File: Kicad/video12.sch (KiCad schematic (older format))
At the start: 18 parts, among them J401 DE15HD, U401 THS7316, U402 TPD7S019

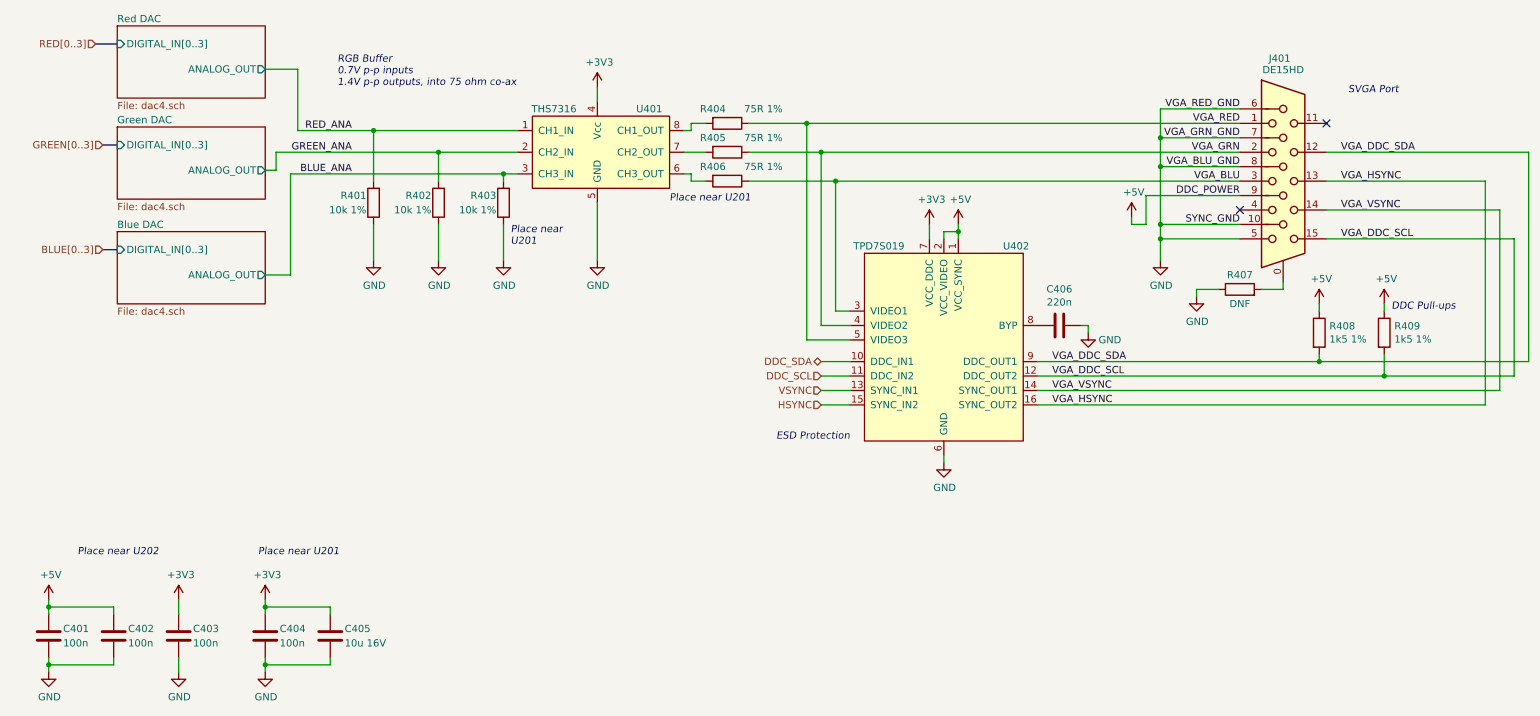
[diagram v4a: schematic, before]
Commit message: BoM and PCB fixes.
* Move tolerances and voltages out of value and into their own fields.
* Fix 5V trace for audio stage.
* Fixup docs.yml so outputs work for JLCPCB.
* Fix JLCPCB part number for 22pF caps.
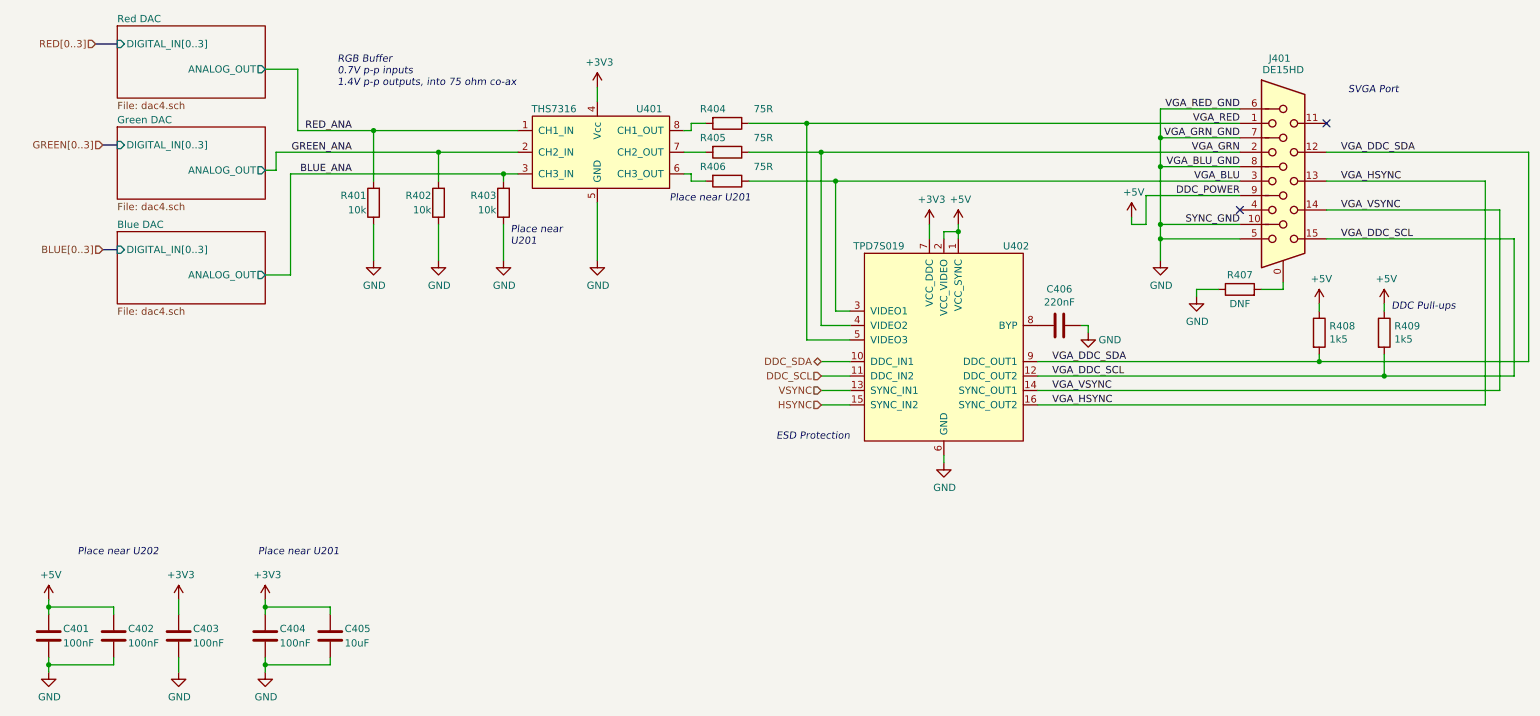
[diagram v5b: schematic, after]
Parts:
- C401, C402, C403, C404: value 100n -> 100nF
- C405: value 10u 16V -> 10uF
- C406: value 220n -> 220nF
- R401, R402, R403: value 10k 1% -> 10k
- R404, R405, R406: value 75R 1% -> 75R
- R408, R409: value 1k5 1% -> 1k5
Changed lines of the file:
@@
 P 5500 3600
 F 0 "R404" V 5400 3500 50  0000 C CNN
-F 1 "75R 1%" V 5400 3850 50  0000 C CNN
+F 1 "75R" V 5400 3850 50  0000 C CNN
 F 2 "Resistor_SMD:R_0805_2012Metric_Pad1.20x1.40mm_HandSolder" V 5430 3600 50  0001 C CNN
 F 3 "~" H 5500 3600 50  0001 C CNN
@@
 P 5500 3800
 F 0 "R405" V 5400 3700 50  0000 C CNN
-F 1 "75R 1%" V 5400 4050 50  0000 C CNN
+F 1 "75R" V 5400 4050 50  0000 C CNN
 F 2 "Resistor_SMD:R_0805_2012Metric_Pad1.20x1.40mm_HandSolder" V 5430 3800 50  0001 C CNN
 F 3 "~" H 5500 3800 50  0001 C CNN
@@
 P 5500 4000
 F 0 "R406" V 5400 3900 50  0000 C CNN
-F 1 "75R 1%" V 5400 4250 50  0000 C CNN
+F 1 "75R" V 5400 4250 50  0000 C CNN
 F 2 "Resistor_SMD:R_0805_2012Metric_Pad1.20x1.40mm_HandSolder" V 5430 4000 50  0001 C CNN
 F 3 "~" H 5500 4000 50  0001 C CNN
@@
 P 3050 4150
 F 0 "R401" H 3100 4100 50  0000 L CNN
-F 1 "10k 1%" H 3100 4200 50  0000 L CNN
+F 1 "10k" H 3100 4200 50  0000 L CNN
 F 2 "Resistor_SMD:R_0805_2012Metric_Pad1.20x1.40mm_HandSolder" V 2980 4150 50  0001 C CNN
 F 3 "~" H 3050 4150 50  0001 C CNN
@@
 P 3500 4150
 F 0 "R402" H 3550 4100 50  0000 L CNN
-F 1 "10k 1%" H 3550 4200 50  0000 L CNN
+F 1 "10k" H 3550 4200 50  0000 L CNN
 F 2 "Resistor_SMD:R_0805_2012Metric_Pad1.20x1.40mm_HandSolder" V 3430 4150 50  0001 C CNN
 F 3 "~" H 3500 4150 50  0001 C CNN
@@
 P 3950 4150
 F 0 "R403" H 4000 4100 50  0000 L CNN
-F 1 "10k 1%" H 4000 4200 50  0000 L CNN
+F 1 "10k" H 4000 4200 50  0000 L CNN
 F 2 "Resistor_SMD:R_0805_2012Metric_Pad1.20x1.40mm_HandSolder" V 3880 4150 50  0001 C CNN
 F 3 "~" H 3950 4150 50  0001 C CNN
@@
 P 9600 5050
 F 0 "R408" H 9670 5096 50  0000 L CNN
-F 1 "1k5 1%" H 9670 5005 50  0000 L CNN
+F 1 "1k5" H 9670 5005 50  0000 L CNN
 F 2 "Resistor_SMD:R_0805_2012Metric_Pad1.20x1.40mm_HandSolder" V 9530 5050 50  0001 C CNN
 F 3 "~" H 9600 5050 50  0001 C CNN
@@
 P 10050 5050
 F 0 "R409" H 10120 5096 50  0000 L CNN
-F 1 "1k5 1%" H 10120 5005 50  0000 L CNN
+F 1 "1k5" H 10120 5005 50  0000 L CNN
 F 2 "Resistor_SMD:R_0805_2012Metric_Pad1.20x1.40mm_HandSolder" V 9980 5050 50  0001 C CNN
 F 3 "~" H 10050 5050 50  0001 C CNN
@@
 P 7800 5000
 F 0 "C406" V 7548 5000 50  0000 C CNN
-F 1 "220n" V 7639 5000 50  0000 C CNN
+F 1 "220nF" V 7639 5000 50  0000 C CNN
 F 2 "Capacitor_SMD:C_0805_2012Metric_Pad1.18x1.45mm_HandSolder" H 7838 4850 50  0001 C CNN
 F 3 "~" H 7800 5000 50  0001 C CNN
@@
 P 800 7150
 F 0 "C401" H 700 7100 50  0000 R CNN
-F 1 "100n" H 700 7200 50  0000 R CNN
+F 1 "100nF" H 700 7200 50  0000 R CNN
 F 2 "Capacitor_SMD:C_0805_2012Metric_Pad1.18x1.45mm_HandSolder" H 838 7000 50  0001 C CNN
 F 3 "~" H 800 7150 50  0001 C CNN
@@
 P 1250 7150
 F 0 "C402" H 1150 7100 50  0000 R CNN
-F 1 "100n" H 1150 7200 50  0000 R CNN
+F 1 "100nF" H 1150 7200 50  0000 R CNN
 F 2 "Capacitor_SMD:C_0805_2012Metric_Pad1.18x1.45mm_HandSolder" H 1288 7000 50  0001 C CNN
 F 3 "~" H 1250 7150 50  0001 C CNN
@@
 P 2300 7150
 F 0 "C404" H 2200 7100 50  0000 R CNN
-F 1 "100n" H 2200 7200 50  0000 R CNN
+F 1 "100nF" H 2200 7200 50  0000 R CNN
 F 2 "Capacitor_SMD:C_0805_2012Metric_Pad1.18x1.45mm_HandSolder" H 2338 7000 50  0001 C CNN
 F 3 "~" H 2300 7150 50  0001 C CNN
@@
 P 2750 7150
 F 0 "C405" H 2650 7200 50  0000 R CNN
-F 1 "10u 16V" H 2650 7100 50  0000 R CNN
+F 1 "10uF" H 2650 7100 50  0000 R CNN
 F 2 "Capacitor_SMD:C_0805_2012Metric_Pad1.18x1.45mm_HandSolder" H 2788 7000 50  0001 C CNN
 F 3 "~" H 2750 7150 50  0001 C CNN
@@
 P 1700 7150
 F 0 "C403" H 1600 7100 50  0000 R CNN
-F 1 "100n" H 1600 7200 50  0000 R CNN
+F 1 "100nF" H 1600 7200 50  0000 R CNN
 F 2 "Capacitor_SMD:C_0805_2012Metric_Pad1.18x1.45mm_HandSolder" H 1738 7000 50  0001 C CNN
 F 3 "~" H 1700 7150 50  0001 C CNN

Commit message: Bugfix/replace vga connector (#20)
* Starting to replace VGA connector.

The Amphenol connectors used on Monotron and the Neotron 32 have a
roughly 8.5mm offset to the board edge. Fixing this will involve moving
a lot of stuff.

* Finish adding new VGA connector.

Had to bunch up the R2R DACs a bit, but overall
it seems tidier this time!
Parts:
- J401: footprint Connector_Dsub:DSUB-15-HD_Female_Horizontal_P2.29x1.98mm_EdgePinOffset3.03mm_Housed_MountingHolesOffset4.94mm -> neotron-pico:Amphenol_ICD15S13E4GV00LF
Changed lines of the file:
@@
 F 0 "J401" H 9250 4850 50  0000 L CNN
 F 1 "DE15HD" H 9350 4800 50  0000 C TNN
-F 2 "Connector_Dsub:DSUB-15-HD_Female_Horizontal_P2.29x1.98mm_EdgePinOffset3.03mm_Housed_MountingHolesOffset4.94mm" H 8400 4400 50  0001 C CNN
+F 2 "neotron-pico:Amphenol_ICD15S13E4GV00LF" H 8400 4400 50  0001 C CNN
 F 3 "~" H 8400 4400 50  0001 C CNN
 F 4 "0" H 9350 4000 50  0001 C CNN "DNP"

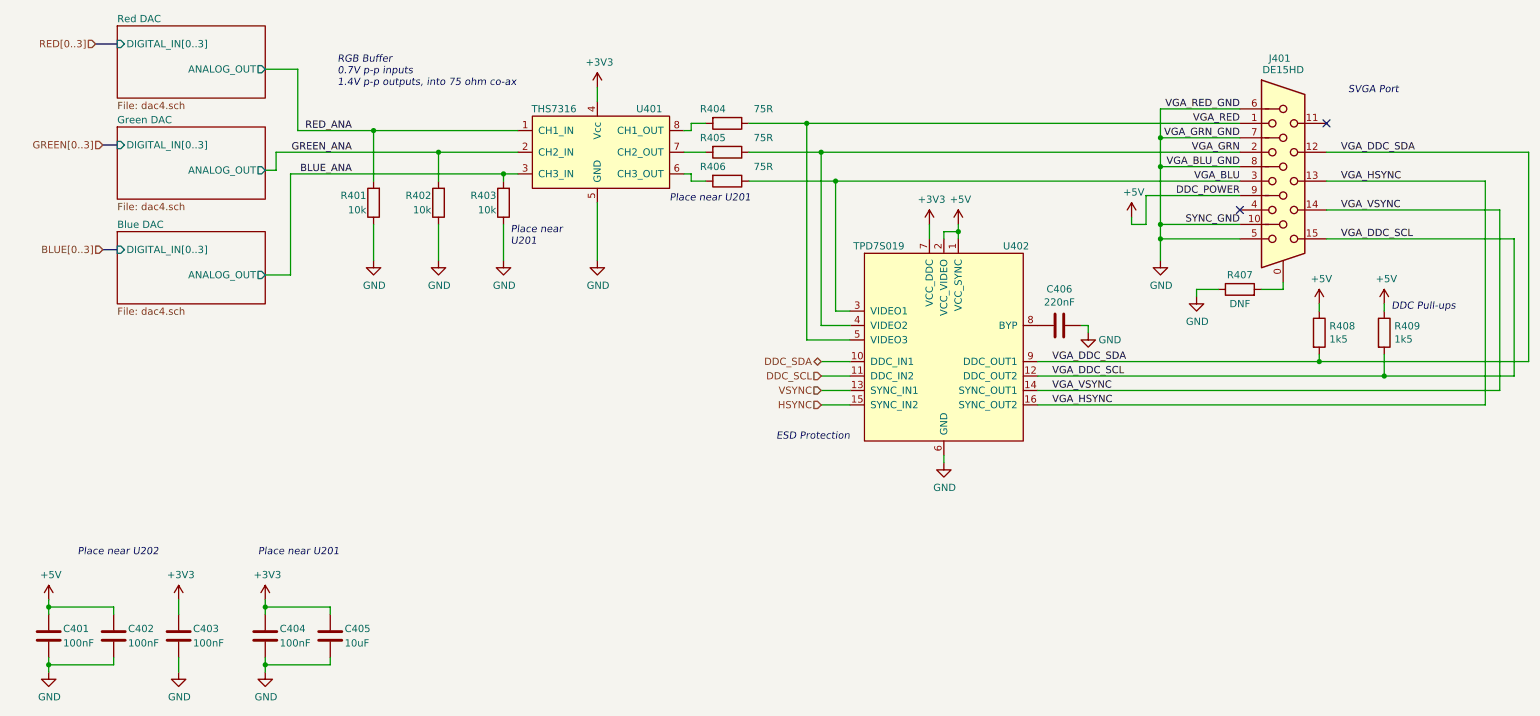
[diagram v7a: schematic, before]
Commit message: Update component values.
Tolerance and Voltage are set to the minimum acceptable. The selected
parts can be better, where a better part is cheaper or has
better availability.

Also dropped R2R DAC tolerance to 1% - 0.5% was overkill. The output
resistor had the wrong value too, which is fixed.
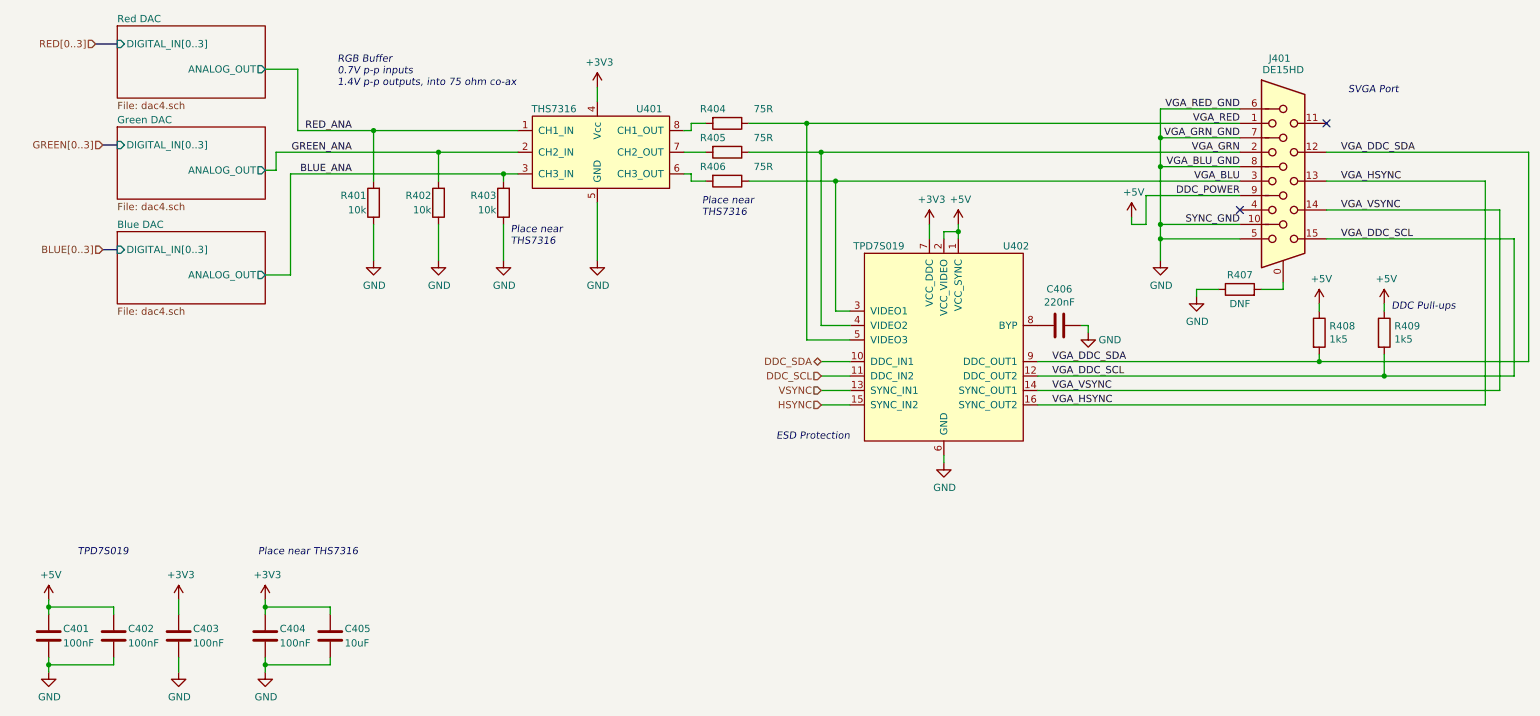
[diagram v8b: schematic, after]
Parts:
- C401, C402: Tolerance (none) -> X5R; Voltage (none) -> 16V
- C403, C404, C405: Tolerance (none) -> X5R; Voltage (none) -> 10V
- C406: Tolerance (none) -> X5R; Voltage (none) -> 50V
- R401, R402, R403, R404, R405, R406, R408, R409: Tolerance (none) -> 1%
- U401: MPN THS7316 -> THS7316DR
- U402: MPN TPD7S019 -> TPD7S019-15DBQR
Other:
- note added: "Place near THS7316"
- note added: "Place near\nTHS7316"
- note added: "TPD7S019"
- note removed: "Place near U201"
- note removed: "Place near U202"
- note removed: "Place near\nU201"
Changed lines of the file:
@@
 F 8 "649-ICD15S13E4GV00LF" H 9350 4000 50  0001 C CNN "Mouser"
 F 9 "~" H 9350 4000 50  0001 C CNN "LCSC Part#"
+F 10 "~" H 9350 4000 50  0001 C CNN "Tolerance"
+F 11 "~" H 9350 4000 50  0001 C CNN "Voltage"
 	1    9350 4000
 	1    0    0    -1
@@
 F 7 "Stackpole" H 5500 3600 50  0001 C CNN "Manufacturer"
 F 8 "C20638" H 5500 3600 50  0001 C CNN "LCSC Part#"
+F 9 "1%" H 5500 3600 50  0001 C CNN "Tolerance"
+F 10 "~" H 5500 3600 50  0001 C CNN "Voltage"
 	1    5500 3600
 	0    1    1    0
@@
 F 7 "Stackpole" H 5500 3800 50  0001 C CNN "Manufacturer"
 F 8 "C20638" H 5500 3800 50  0001 C CNN "LCSC Part#"
+F 9 "1%" H 5500 3800 50  0001 C CNN "Tolerance"
+F 10 "~" H 5500 3800 50  0001 C CNN "Voltage"
 	1    5500 3800
 	0    1    1    0
@@
 F 7 "Stackpole" H 5500 4000 50  0001 C CNN "Manufacturer"
 F 8 "C20638" H 5500 4000 50  0001 C CNN "LCSC Part#"
+F 9 "1%" H 5500 4000 50  0001 C CNN "Tolerance"
+F 10 "~" H 5500 4000 50  0001 C CNN "Voltage"
 	1    5500 4000
 	0    1    1    0
@@
 F 3 "~" H 3050 4150 50  0001 C CNN
 F 4 "0" H 3050 4150 50  0001 C CNN "DNP"
-F 5 "" H 3050 4150 50  0001 C CNN "Digikey"
+F 5 "~" H 3050 4150 50  0001 C CNN "Digikey"
 F 6 "CPL-RES-0805-10K-0.125W" H 3050 4150 50  0001 C CNN "MPN"
 F 7 "CPL" H 3050 4150 50  0001 C CNN "Manufacturer"
 F 8 "C17414" H 3050 4150 50  0001 C CNN "LCSC Part#"
+F 9 "1%" H 3050 4150 50  0001 C CNN "Tolerance"
+F 10 "~" H 3050 4150 50  0001 C CNN "Mouser"
+F 11 "~" H 3050 4150 50  0001 C CNN "Voltage"
 	1    3050 4150
 	-1   0    0    1
@@
 F 3 "~" H 3500 4150 50  0001 C CNN
 F 4 "0" H 3500 4150 50  0001 C CNN "DNP"
-F 5 "" H 3500 4150 50  0001 C CNN "Digikey"
+F 5 "~" H 3500 4150 50  0001 C CNN "Digikey"
 F 6 "CPL-RES-0805-10K-0.125W" H 3500 4150 50  0001 C CNN "MPN"
 F 7 "CPL" H 3500 4150 50  0001 C CNN "Manufacturer"
 F 8 "C17414" H 3500 4150 50  0001 C CNN "LCSC Part#"
+F 9 "1%" H 3500 4150 50  0001 C CNN "Tolerance"
+F 10 "~" H 3500 4150 50  0001 C CNN "Mouser"
+F 11 "~" H 3500 4150 50  0001 C CNN "Voltage"
 	1    3500 4150
 	-1   0    0    1
@@
 F 3 "~" H 3950 4150 50  0001 C CNN
 F 4 "0" H 3950 4150 50  0001 C CNN "DNP"
-F 5 "" H 3950 4150 50  0001 C CNN "Digikey"
+F 5 "~" H 3950 4150 50  0001 C CNN "Digikey"
 F 6 "CPL-RES-0805-10K-0.125W" H 3950 4150 50  0001 C CNN "MPN"
 F 7 "CPL" H 3950 4150 50  0001 C CNN "Manufacturer"
 F 8 "C17414" H 3950 4150 50  0001 C CNN "LCSC Part#"
+F 9 "1%" H 3950 4150 50  0001 C CNN "Tolerance"
+F 10 "~" H 3950 4150 50  0001 C CNN "Mouser"
+F 11 "~" H 3950 4150 50  0001 C CNN "Voltage"
 	1    3950 4150
 	-1   0    0    1
@@
 F 3 "https://www.ti.com/lit/ds/symlink/tpd7s019.pdf" H 7550 5200 50  0001 C CNN
 F 4 "Texas Instruments" H 7000 3750 50  0001 C CNN "Manufacturer"
-F 5 "TPD7S019" H 7000 3650 50  0001 C CNN "MPN"
+F 5 "TPD7S019-15DBQR" H 7000 3650 50  0001 C CNN "MPN"
 F 6 "0" H 7000 5100 50  0001 C CNN "DNP"
 F 7 "296-27595-1-ND" H 7000 5100 50  0001 C CNN "Digikey"
 F 8 "595-TPD7S019-15DBQR" H 7000 5100 50  0001 C CNN "Mouser"
 F 9 "C337499" H 7000 5100 50  0001 C CNN "LCSC Part#"
+F 10 "~" H 7000 5100 50  0001 C CNN "Tolerance"
+F 11 "~" H 7000 5100 50  0001 C CNN "Voltage"
 	1    7000 5100
 	1    0    0    -1
@@
 F 5 "0" H 4750 3800 50  0001 C CNN "DNP"
 F 6 "296-26684-1-ND" H 4750 3800 50  0001 C CNN "Digikey"
-F 7 "THS7316" H 4750 3800 50  0001 C CNN "MPN"
+F 7 "THS7316DR" H 4750 3800 50  0001 C CNN "MPN"
 F 8 "595-THS7316DR" H 4750 3800 50  0001 C CNN "Mouser"
 F 9 "C155446" H 4750 3800 50  0001 C CNN "LCSC Part#"
+F 10 "~" H 4750 3800 50  0001 C CNN "Tolerance"
+F 11 "~" H 4750 3800 50  0001 C CNN "Voltage"
 	1    4750 3800
 	1    0    0    -1
@@
 F 7 "Stackpole" H 9600 5050 50  0001 C CNN "Manufacturer"
 F 8 "C4310" H 9600 5050 50  0001 C CNN "LCSC Part#"
+F 9 "1%" H 9600 5050 50  0001 C CNN "Tolerance"
+F 10 "~" H 9600 5050 50  0001 C CNN "Voltage"
 	1    9600 5050
 	1    0    0    -1
@@
 F 7 "Stackpole" H 10050 5050 50  0001 C CNN "Manufacturer"
 F 8 "C4310" H 10050 5050 50  0001 C CNN "LCSC Part#"
+F 9 "1%" H 10050 5050 50  0001 C CNN "Tolerance"
+F 10 "~" H 10050 5050 50  0001 C CNN "Voltage"
 	1    10050 5050
 	1    0    0    -1
@@
 F 7 "Samsung" H 7800 5000 50  0001 C CNN "Manufacturer"
 F 8 "C5378" H 7800 5000 50  0001 C CNN "LCSC Part#"
+F 9 "X5R" H 7800 5000 50  0001 C CNN "Tolerance"
+F 10 "50V" H 7800 5000 50  0001 C CNN "Voltage"
+F 11 "~" H 7800 5000 50  0001 C CNN "Mouser"
 	1    7800 5000
 	0    1    1    0
@@
 F 3 "~" H 800 7150 50  0001 C CNN
 F 4 "0" H 800 7150 50  0001 C CNN "DNP"
-F 5 "" H 800 7150 50  0001 C CNN "Digikey"
+F 5 "~" H 800 7150 50  0001 C CNN "Digikey"
 F 6 "CPL-CAP-X7R-0805-100NF-50V" H 800 7150 50  0001 C CNN "MPN"
 F 7 "CPL" H 800 7150 50  0001 C CNN "Manufacturer"
-F 8 "" H 800 7150 50  0001 C CNN "Mouser"
+F 8 "~" H 800 7150 50  0001 C CNN "Mouser"
 F 9 "C49678" H 800 7150 50  0001 C CNN "LCSC Part#"
+F 10 "X5R" H 800 7150 50  0001 C CNN "Tolerance"
+F 11 "16V" H 800 7150 50  0001 C CNN "Voltage"
 	1    800  7150
 	-1   0    0    1
@@
 F 3 "~" H 1250 7150 50  0001 C CNN
 F 4 "0" H 1250 7150 50  0001 C CNN "DNP"
-F 5 "" H 1250 7150 50  0001 C CNN "Digikey"
+F 5 "~" H 1250 7150 50  0001 C CNN "Digikey"
 F 6 "CPL-CAP-X7R-0805-100NF-50V" H 1250 7150 50  0001 C CNN "MPN"
 F 7 "CPL" H 1250 7150 50  0001 C CNN "Manufacturer"
-F 8 "" H 1250 7150 50  0001 C CNN "Mouser"
+F 8 "~" H 1250 7150 50  0001 C CNN "Mouser"
 F 9 "C49678" H 1250 7150 50  0001 C CNN "LCSC Part#"
+F 10 "X5R" H 1250 7150 50  0001 C CNN "Tolerance"
+F 11 "16V" H 1250 7150 50  0001 C CNN "Voltage"
 	1    1250 7150
 	-1   0    0    1
@@
 $EndComp
 Text Notes 1000 6600 0    50   Italic 0
-Place near U202
+TPD7S019
 Text Notes 2250 6600 0    50   Italic 0
-Place near U201
+Place near THS7316
 $Comp
 L power:+3V3 #PWR0405
@@
 F 3 "~" H 2300 7150 50  0001 C CNN
 F 4 "0" H 2300 7150 50  0001 C CNN "DNP"
-F 5 "" H 2300 7150 50  0001 C CNN "Digikey"
+F 5 "~" H 2300 7150 50  0001 C CNN "Digikey"
 F 6 "CPL-CAP-X7R-0805-100NF-50V" H 2300 7150 50  0001 C CNN "MPN"
 F 7 "CPL" H 2300 7150 50  0001 C CNN "Manufacturer"
-F 8 "" H 2300 7150 50  0001 C CNN "Mouser"
+F 8 "~" H 2300 7150 50  0001 C CNN "Mouser"
 F 9 "C49678" H 2300 7150 50  0001 C CNN "LCSC Part#"
+F 10 "X5R" H 2300 7150 50  0001 C CNN "Tolerance"
+F 11 "10V" H 2300 7150 50  0001 C CNN "Voltage"
 	1    2300 7150
 	-1   0    0    1
@@
 F 3 "~" H 2750 7150 50  0001 C CNN
 F 4 "0" H 2750 7150 50  0001 C CNN "DNP"
-F 5 "" H 2750 7150 50  0001 C CNN "Digikey"
+F 5 "~" H 2750 7150 50  0001 C CNN "Digikey"
 F 6 "CPL-CAP-X5R-0805-10UF-16V" H 2750 7150 50  0001 C CNN "MPN"
 F 7 "CPL" H 2750 7150 50  0001 C CNN "Manufacturer"
 F 8 "C15850" H 2750 7150 50  0001 C CNN "LCSC Part#"
+F 9 "X5R" H 2750 7150 50  0001 C CNN "Tolerance"
+F 10 "10V" H 2750 7150 50  0001 C CNN "Voltage"
+F 11 "~" H 2750 7150 50  0001 C CNN "Mouser"
 	1    2750 7150
 	-1   0    0    -1
@@
 F 6 "~" H 9050 4750 50  0001 C CNN "MPN"
 F 7 "~" H 9050 4750 50  0001 C CNN "Manufacturer"
-F 8 "" H 9050 4750 50  0001 C CNN "Mouser"
+F 8 "~" H 9050 4750 50  0001 C CNN "Mouser"
 F 9 "~" H 9050 4750 50  0001 C CNN "LCSC Part#"
+F 10 "~" H 9050 4750 50  0001 C CNN "Tolerance"
+F 11 "~" H 9050 4750 50  0001 C CNN "Voltage"
 	1    9050 4750
 	0    -1   -1   0
@@
 Wire Wire Line
 	8000 5000 8000 5050
-Text Notes 5100 4150 0    50   Italic 0
-Place near U201
+Text Notes 5325 4250 0    50   Italic 0
+Place near\nTHS7316
 Text Notes 4000 4450 0    50   Italic 0
-Place near\nU201
+Place near\nTHS7316
 Text Label 2900 3650 2    50   ~ 0
 RED_ANA
@@
 F 3 "~" H 1700 7150 50  0001 C CNN
 F 4 "0" H 1700 7150 50  0001 C CNN "DNP"
-F 5 "" H 1700 7150 50  0001 C CNN "Digikey"
+F 5 "~" H 1700 7150 50  0001 C CNN "Digikey"
 F 6 "CPL-CAP-X7R-0805-100NF-50V" H 1700 7150 50  0001 C CNN "MPN"
 F 7 "CPL" H 1700 7150 50  0001 C CNN "Manufacturer"
-F 8 "" H 1700 7150 50  0001 C CNN "Mouser"
+F 8 "~" H 1700 7150 50  0001 C CNN "Mouser"
 F 9 "C49678" H 1700 7150 50  0001 C CNN "LCSC Part#"
+F 10 "X5R" H 1700 7150 50  0001 C CNN "Tolerance"
+F 11 "10V" H 1700 7150 50  0001 C CNN "Voltage"
 	1    1700 7150
 	-1   0    0    1
